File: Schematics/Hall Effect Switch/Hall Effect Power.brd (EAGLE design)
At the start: 7.6 x 22.4 mm, 8 parts

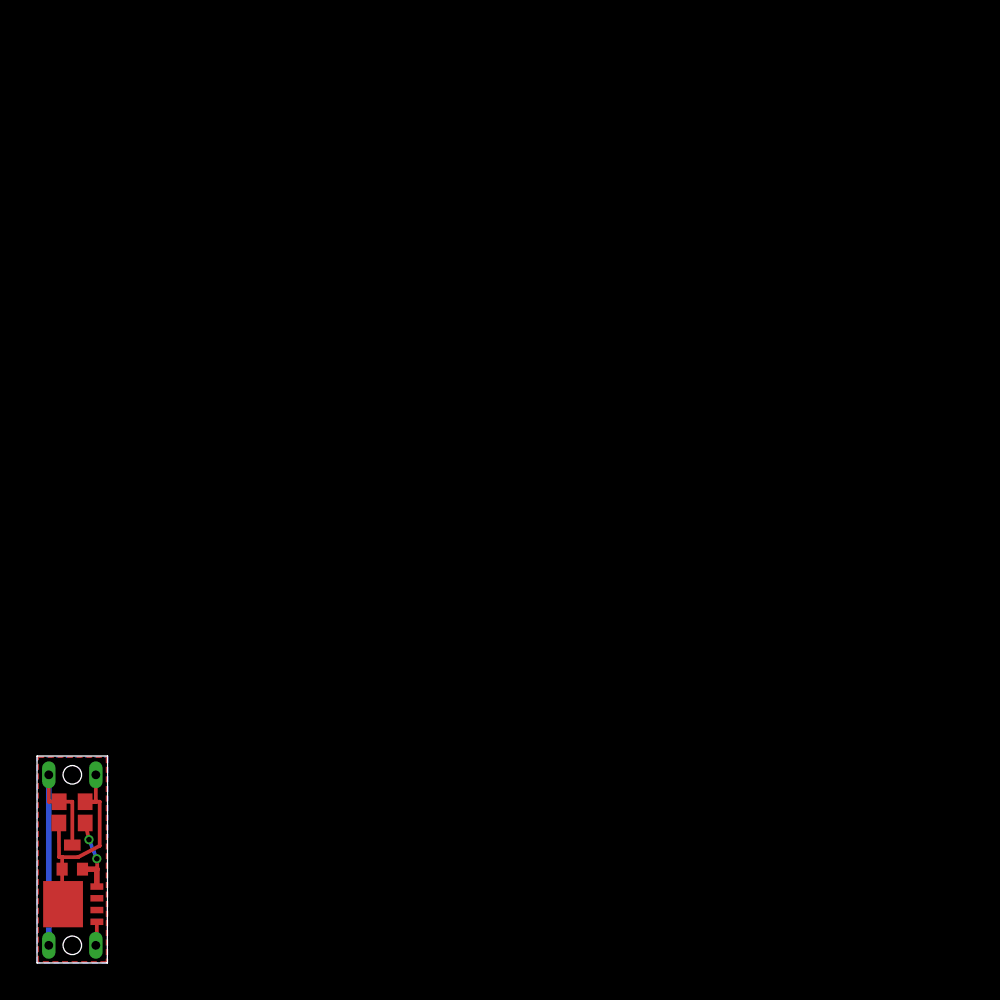
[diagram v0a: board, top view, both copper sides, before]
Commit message: New Hall Effect Switch
Changed all the parts for the hall effect switch.
The goal is lower passive power consumption and lower Rds(on).

Panelized the new hall effect switch.
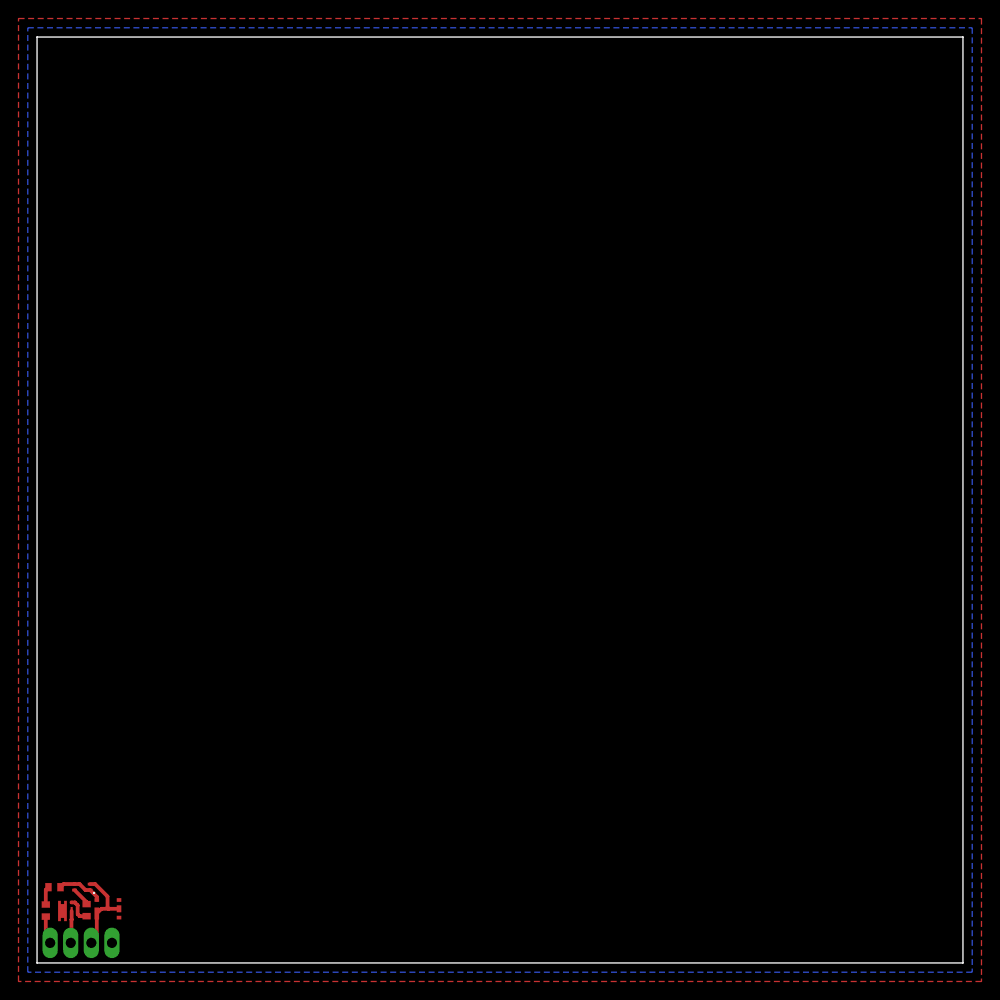
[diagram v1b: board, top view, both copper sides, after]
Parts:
- removed BATTERY+, BATTERY-, OUTPUT+, OUTPUT-: SINGLE_WIRE, ROCKET CLUB:SINGLE_WIRE
- removed C1: (no value), rcl:C1206
- removed IC1: (no value), allegro:SOT23-W
- removed Q1: (no value), transistor-power:SOT669
- removed R1: (no value), resistor:R1206
- added 3.1, 3.3: RESISTORC0402, RocketControlBoard:C0402
- added 4.7UF: CAPACITORC0402, RocketControlBoard:C0402
- added U$1: HALL-MOSFET-NEW, RocketControlBoard:HALL-MOSFET-NEW
- added U$2: HALL-HALL-NEW, RocketControlBoard:HALL-HALL-NEW
- added U$3: HALL-REG-NEW, RocketControlBoard:HALL-REG-NEW
- added U$4, U$5, U$6, U$7: SINGLE-WIRE, RocketControlBoard:SINGLE-WIRE
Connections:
- new net N$1: 4.7UF.2, U$2.CE, U$2.VDD, U$3.4
- new net N$2: 3.3.2, 4.7UF.1
- new net N$3: 3.1.1, U$1.G@1
- net GND: now also 3.3.1, U$2.GND, U$3.2, U$3.5, U$4.P$1, U$7.P$1; no longer BATTERY-.P$1, C1.2, IC1.3, OUTPUT-.P$1
- net HALL_OUT: now also 3.1.2, U$2.OUT; no longer IC1.2, Q1.4, R1.2
- net VIN: now also U$1.D#4, U$1.D@1, U$1.D@2, U$1.D@3, U$1.D@5, U$3.1, U$3.3, U$6.P$1; no longer BATTERY+.P$1, C1.1, IC1.1, Q1.MB, R1.1
- net VIN_OUT: now also U$1.S@1, U$1.S@2, U$5.P$1; no longer OUTPUT+.P$1, Q1.1
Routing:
- net VIN: track 24.0 -> 0.00 mm
- net GND: track 28.5 -> 12.9 mm
- net HALL_OUT: track 10.2 -> 2.06 mm, vias 2 -> 0
- net N$1: track 0.00 -> 4.98 mm
- net N$3: track 0.00 -> 2.81 mm
- net N$2: track 0.00 -> 1.99 mm
- net VIN_OUT: track 2.76 -> 3.48 mm
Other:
- board size 7.6 x 22.4 mm -> 100 x 100 mm
- board text added: "IN +|-"
- board text added: "Magnetic Switch"
- board text added: "OUT +|-"
- board text removed: "+ IN -"
- board text removed: "+ OUT -"
